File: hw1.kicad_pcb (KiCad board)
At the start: 2 copper layers, 148.5 x 66.9 mm, 68 parts, among them J2 USB_C_Receptacle_USB2.0_16P, M1 Stepper_Motor, Q1 STL6P3LLH6, SW1 RotaryEncoder_Switch, SW2 SW_Back, SW5 SW_Bolus, SW6 SW_Settings, U2 STUSB4500QTR, U3 TPS54331DR, U4 XIAO-RP2350-DIP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

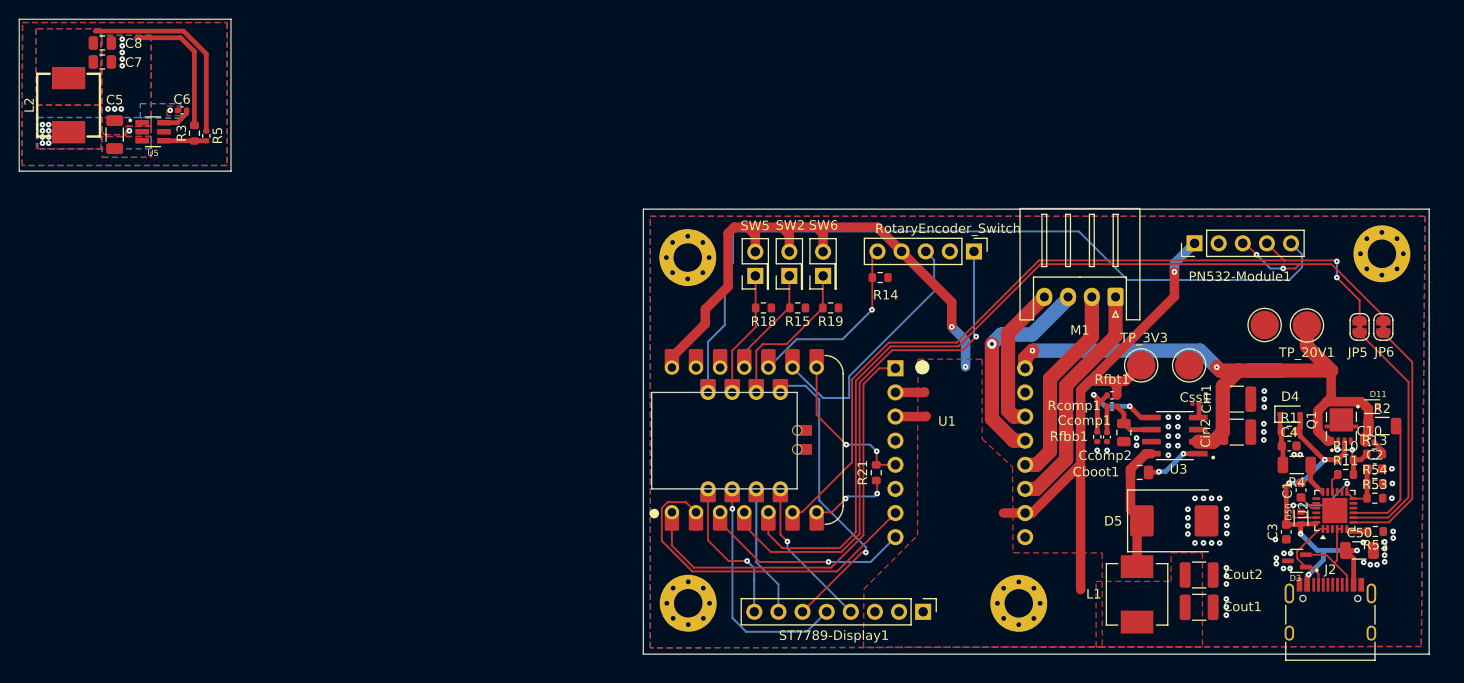
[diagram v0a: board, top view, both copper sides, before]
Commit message: Added thicker traces for the whole MCU part. Still need to fix some DRC errors related to the XIAO's castellated pins.
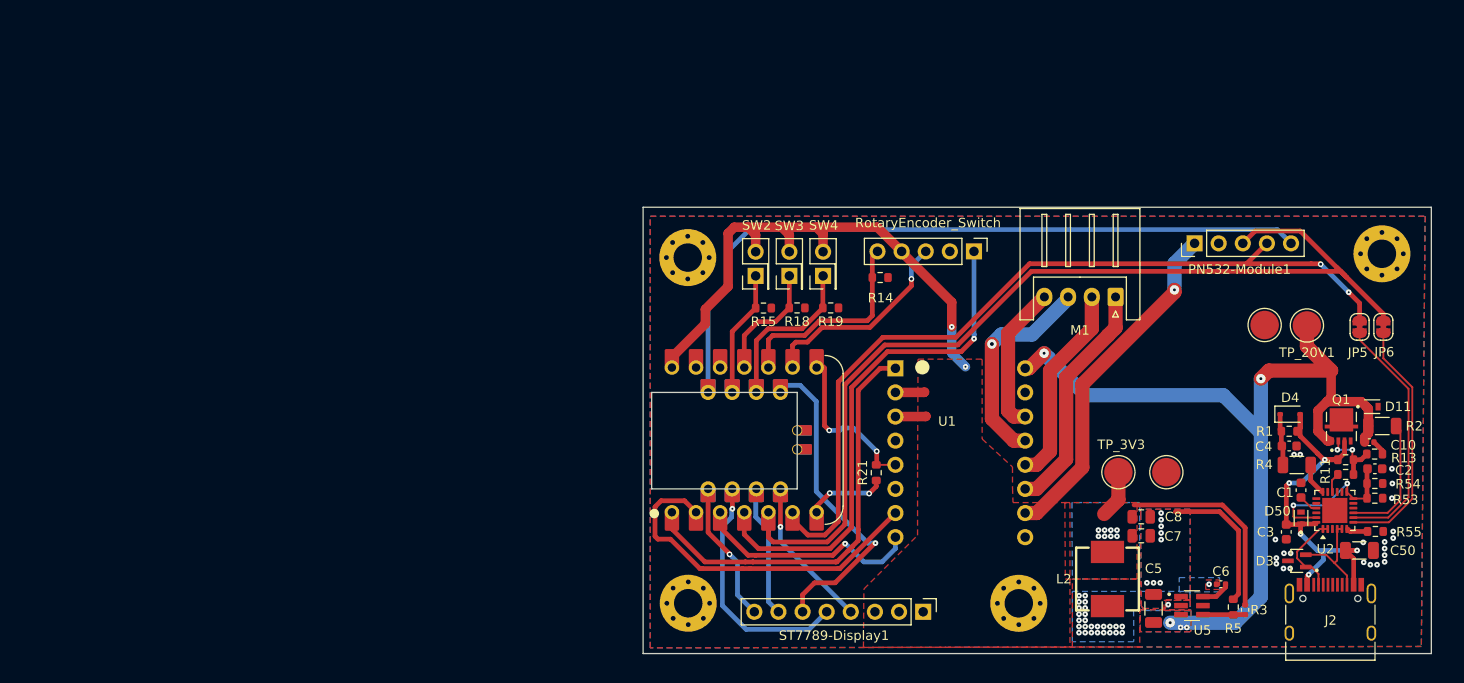
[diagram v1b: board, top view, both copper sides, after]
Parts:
- removed Cboot1: 100nF, Capacitor_SMD:C_0805_2012Metric
- removed Ccomp1: 1nF, Capacitor_SMD:C_0402_1005Metric
- removed Ccomp2: 10pF, Capacitor_SMD:C_0805_2012Metric
- removed Cin1, Cin2: 10uF, Capacitor_SMD:C_1210_3225Metric
- removed Cout1, Cout2: 100uF, Capacitor_SMD:C_1210_3225Metric
- removed Css1: 8.2nF, Capacitor_SMD:C_0201_0603Metric
- removed D5: 550mV 5A, Diode_SMD:D_SMC
- removed L1: 8.2uH, hw1_footprint:IND_IHLP2525CZER8R2M01
- removed Rcomp1: 41.2k, Resistor_SMD:R_0402_1005Metric
- removed Rfbb1: 3.24k, Resistor_SMD:R_0402_1005Metric
- removed Rfbt1: 10.2k, Resistor_SMD:R_0402_1005Metric
- removed U3: TPS54331DR, hw1_footprint:SOIC127P599X175-8N
- moved C5 120.2 mm to (226.7, 138.2)
- moved C6 120.2 mm to (233.8, 135.6)
- moved L2 120.2 mm to (221.8, 135.1)
- moved R3 120.2 mm to (236.3, 138.3)
- moved R5 120.2 mm to (235.1, 138.0)
- moved C7 120.2 mm to (225.3, 130.5)
- moved C8 120.2 mm to (225.3, 128.5)
- moved U5 120.2 mm to (230.7, 137.8)
- moved TP4 11.5 mm to (228.0, 123.8)
- moved TP_3V3 11.5 mm to (222.9, 123.8)
- moved R15 3.60 mm to (185.6, 106.5)
- moved SW3 3.59 mm to (188.3, 103.1)
- moved SW2 3.55 mm to (184.8, 103.1)
- moved R18 3.54 mm to (189.1, 106.5)
- renumbered SW5 to SW3, SW6 to SW4
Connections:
- U4 pad 11: SW_BACK -> SW_BOLUS
- U4 pad 16: SW_BOLUS -> SW_BACK
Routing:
- net +20_USB: track 70.7 -> 93.2 mm, vias 2 -> 5
- net +3.3_BUCK: track 147.9 -> 127.7 mm, vias 3 -> 11
- net Net-(D5-K): track 14.7 -> 0.00 mm
- net Net-(U3-VSENSE): track 12.6 -> 0.00 mm, vias 2 -> 0
- net NFC_IRQ: track 83.0 -> 75.8 mm
- net Net-(U3-BOOT): track 6.06 -> 0.00 mm, vias 2 -> 0
- net ENC_B: track 26.8 -> 20.9 mm, vias 0 -> 1
- net I2C_SDA: track 98.6 -> 104.5 mm, vias 2 -> 0
- net Net-(U3-COMP): track 5.27 -> 0.00 mm
- net I2C_SCL: track 83.4 -> 87.4 mm
- net Net-(Ccomp1-Pad2): track 2.75 -> 0.00 mm
- net D_EN: track 46.0 -> 43.7 mm
- net D_DIR: track 22.3 -> 24.7 mm
- net ST_DC: track 32.1 -> 34.2 mm
- net Net-(U3-SS): track 1.45 -> 0.00 mm
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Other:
- board size 148.5 x 66.9 mm -> 83 x 47 mm

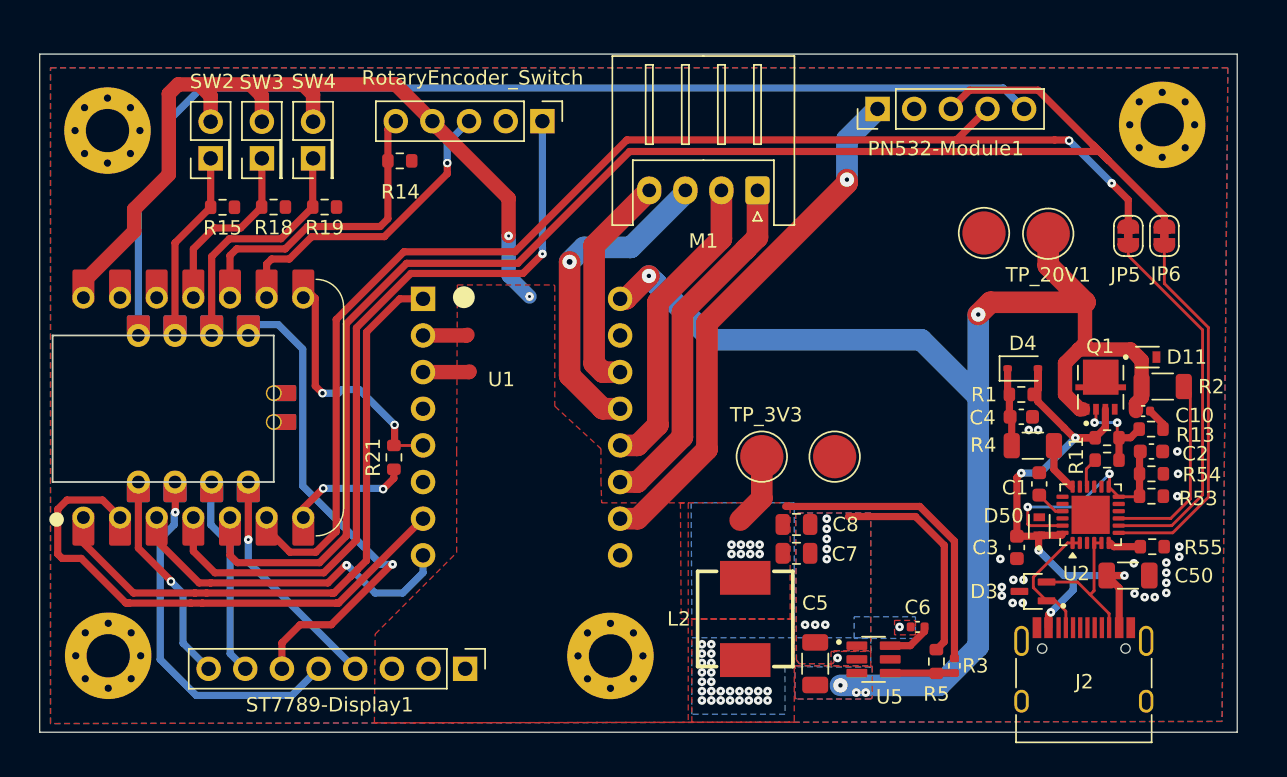
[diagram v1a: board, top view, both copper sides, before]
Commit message: Re-arranged some traces
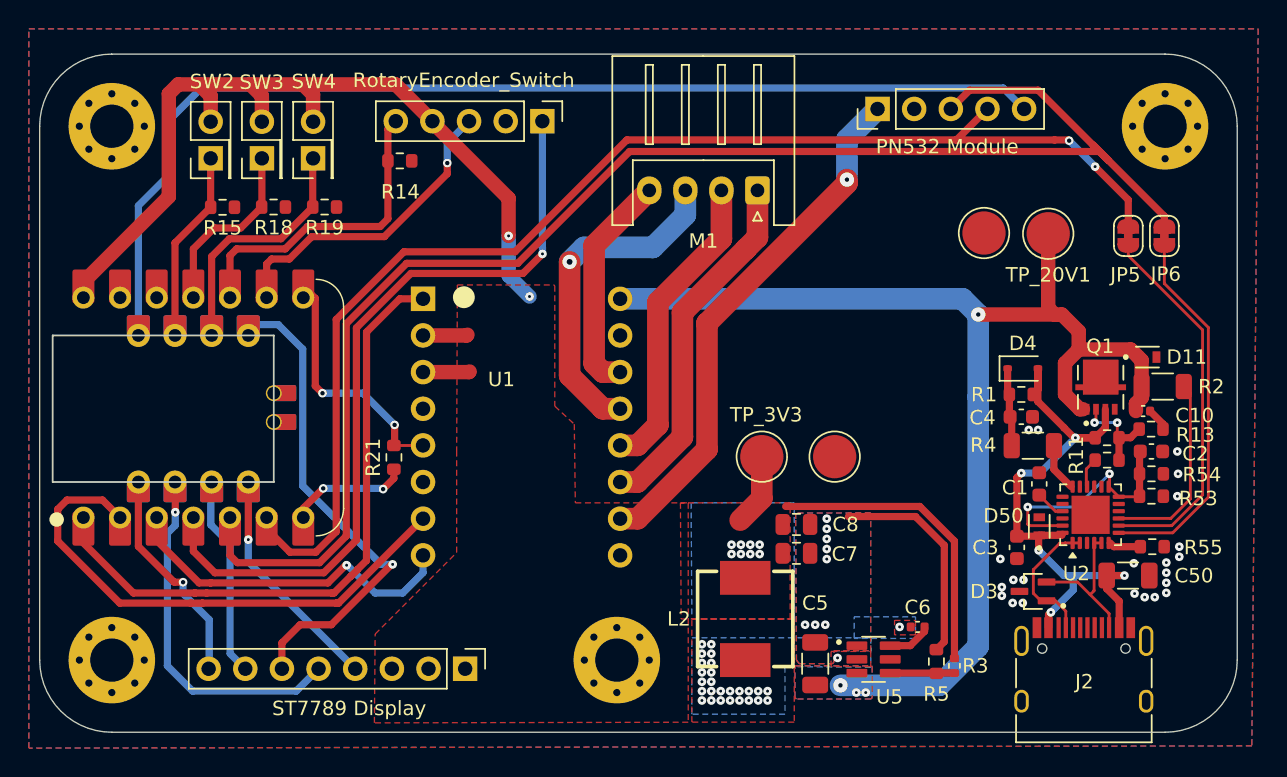
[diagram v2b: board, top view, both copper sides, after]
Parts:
- moved H4 0.53 mm to (212.9, 137.9)
- moved H1 0.42 mm to (177.9, 100.9)
- moved H3 0.39 mm to (177.9, 137.9)
- moved H2 0.22 mm to (250.9, 100.9)
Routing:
- net +20_USB: track 93.2 -> 87.0 mm, vias 5 -> 4
- net M1B: track 22.5 -> 23.4 mm
- net ST_CLK: track 24.9 -> 24.1 mm
- net CC1: track 9.00 -> 9.54 mm
- net D_STEP: track 37.3 -> 36.8 mm
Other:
- outline, holes or cut-outs redrawn
- board text added: "PN532 Module"
- board text added: "RotaryEncoder_Switch"
- board text added: "ST7789 Display"
